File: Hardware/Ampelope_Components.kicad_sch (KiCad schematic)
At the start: 101 parts, among them J1 Conn_01x12_Male, J18 SWD_Header, J19 USB_B_Micro, J2 Conn_01x12_Male, J3 Conn_01x12_Male, J4 Conn_01x12_Male, J5 Eurorack_16_pin_power, Q1 MMBT3904, Q2 MMBT3904, Q3 MMBT3904, Q4 MMBT3904, Q5 MMBT3904, U1 STM32G431RB, U2 AS3364, U3 LM1117-3.3, U4 TL074, U5 TL074, U6 TL074, Y1 8MHz 20pF

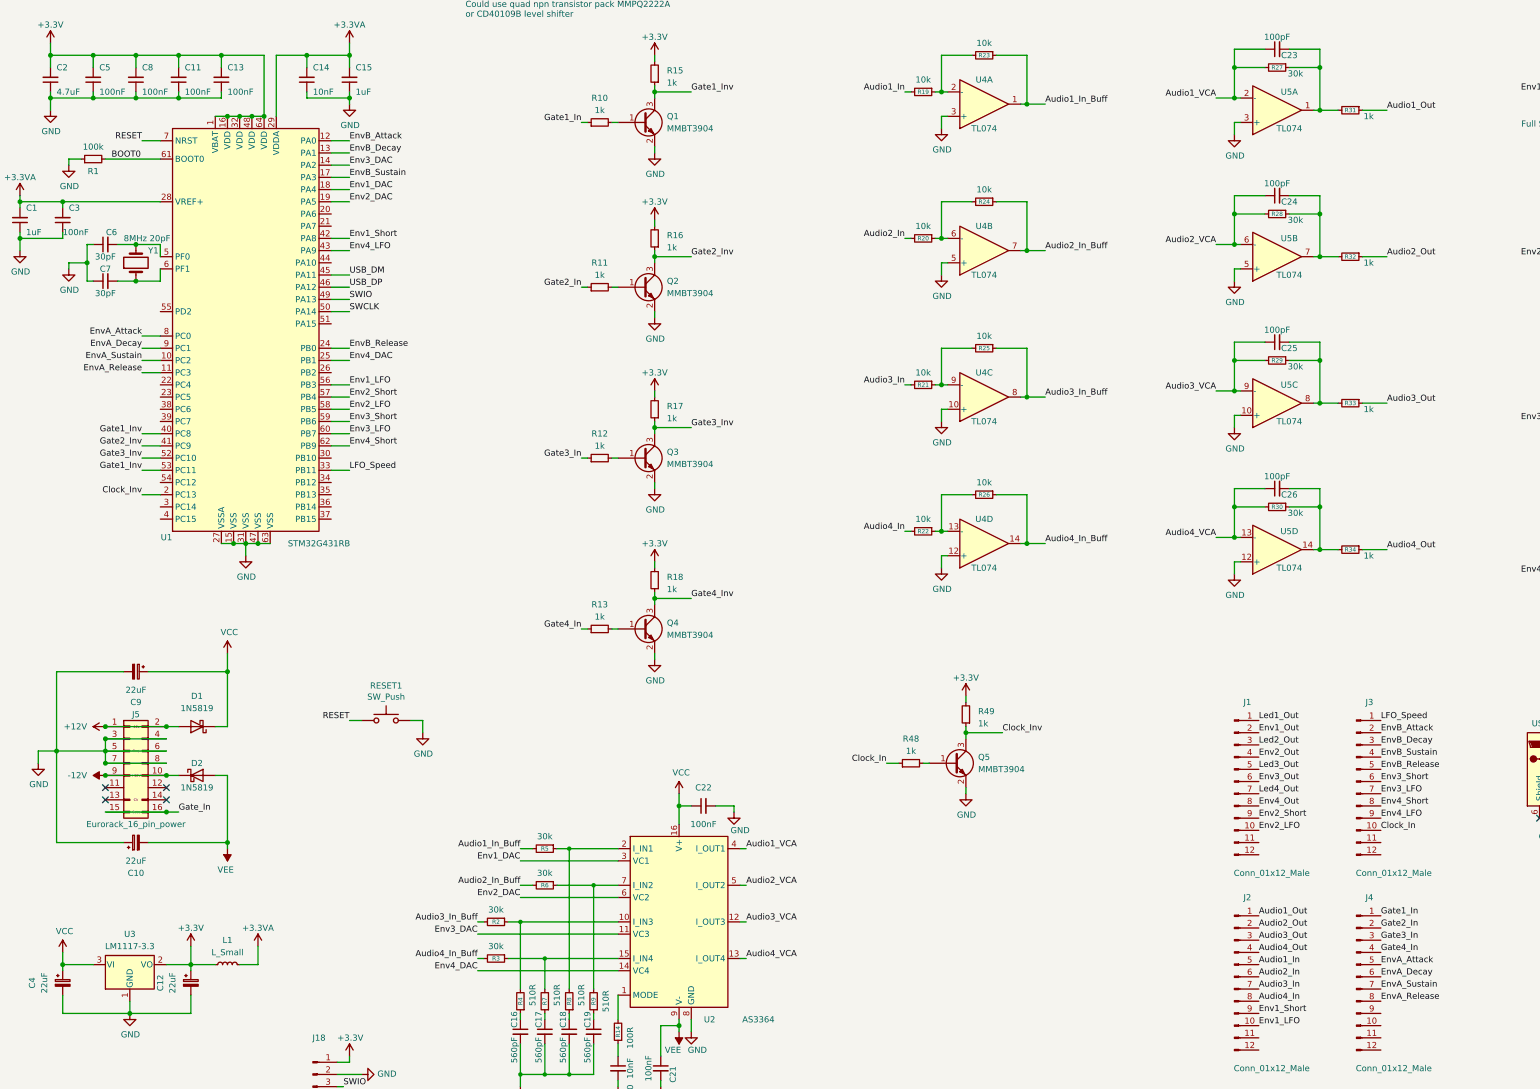
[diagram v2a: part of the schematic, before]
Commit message: More layout on component board
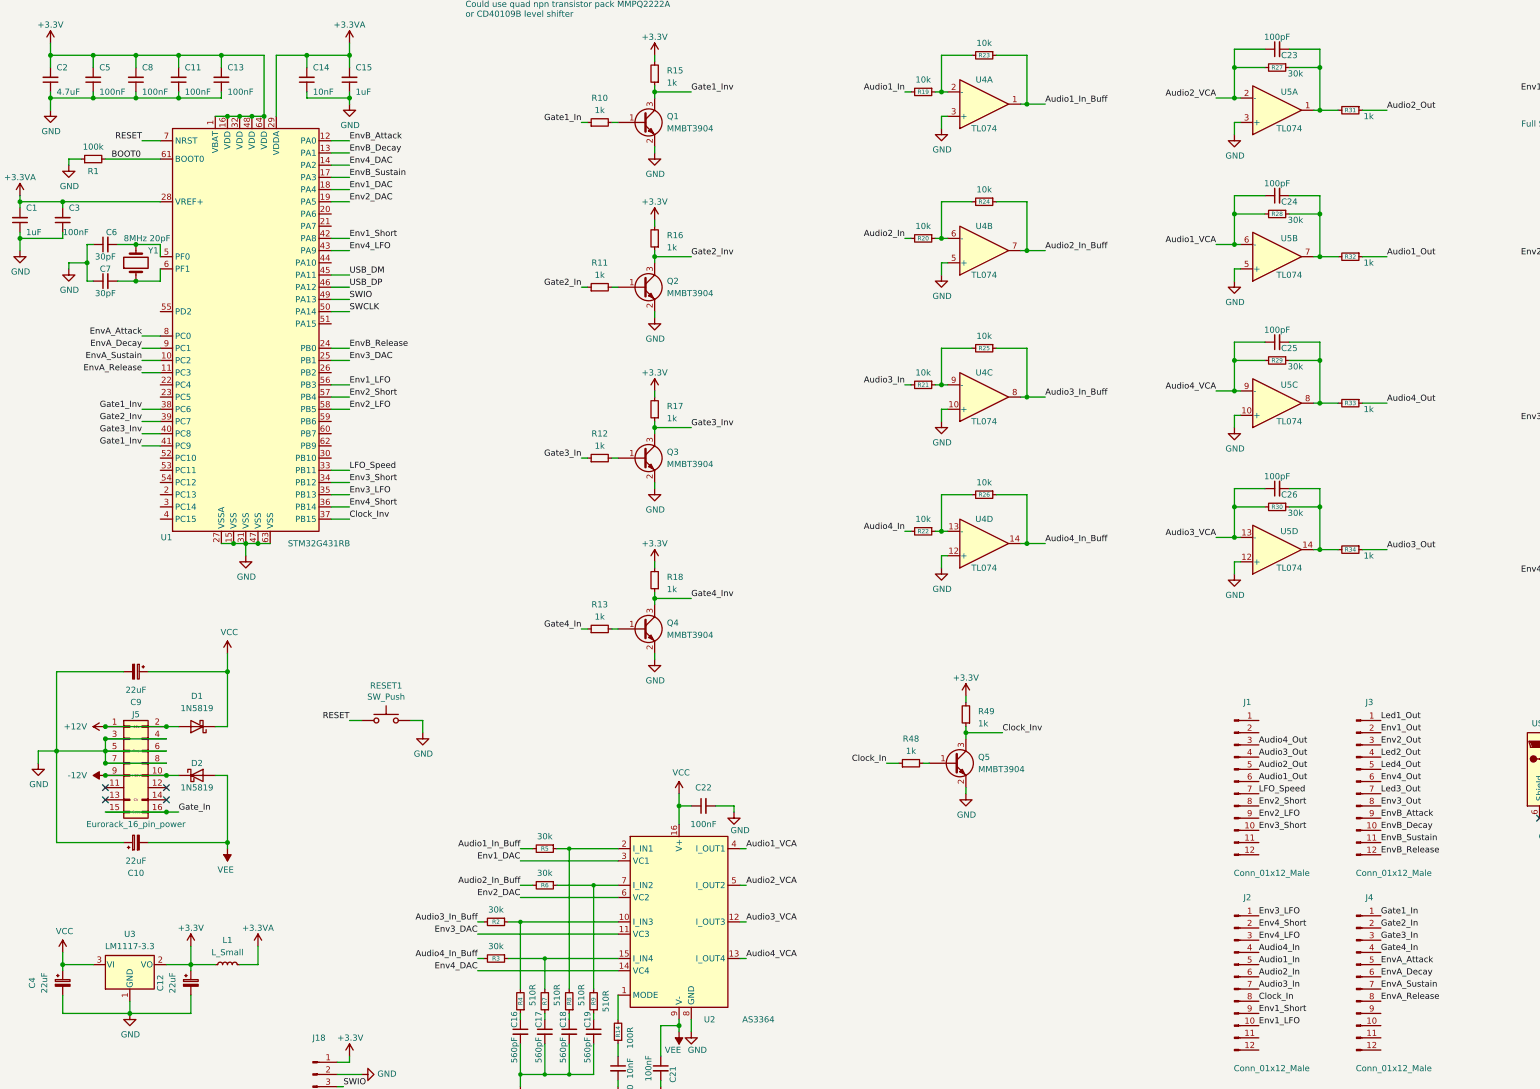
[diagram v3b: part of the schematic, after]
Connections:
- net Audio1_Out: now also J1.6 (Pin_6), R32.1; no longer J2.1 (Pin_1), R31.1
- net Audio1_VCA: now also C24.1, R28.2, U5.6 (-); no longer C23.1, R27.2, U5.2 (-)
- net Audio2_Out: now also J1.5 (Pin_5), R31.1; no longer J2.2 (Pin_2), R32.1
- net Audio2_VCA: now also C23.1, R27.2, U5.2 (-); no longer C24.1, R28.2, U5.6 (-)
- net Audio3_Out: now also J1.4 (Pin_4), R34.1; no longer J2.3 (Pin_3), R33.1
- net Audio3_VCA: now also C26.1, R30.2, U5.13 (-); no longer C25.1, R29.2, U5.9 (-)
- net Audio4_In: now also J2.4 (Pin_4); no longer J2.8 (Pin_8)
- net Audio4_Out: now also J1.3 (Pin_3), R33.1; no longer J2.4 (Pin_4), R34.1
- net Audio4_VCA: now also C25.1, R29.2, U5.9 (-); no longer C26.1, R30.2, U5.13 (-)
- net Clock_In: now also J2.8 (Pin_8); no longer J3.10 (Pin_10)
- net Clock_Inv: now also U1.37 (PB15); no longer U1.2 (PC13)
- net Env1_Out: now also J3.2 (Pin_2); no longer J1.2 (Pin_2)
- net Env2_LFO: now also J1.9 (Pin_9); no longer J1.10 (Pin_10)
- net Env2_Out: now also J3.3 (Pin_3); no longer J1.4 (Pin_4)
- net Env2_Short: now also J1.8 (Pin_8); no longer J1.9 (Pin_9)
- net Env3_DAC: now also U1.25 (PB1); no longer U1.14 (PA2)
- net Env3_LFO: now also J2.1 (Pin_1), U1.35 (PB13); no longer J3.7 (Pin_7), U1.60 (PB7)
- net Env3_Out: now also J3.8 (Pin_8); no longer J1.6 (Pin_6)
- net Env3_Short: now also J1.10 (Pin_10), U1.34 (PB12); no longer J3.6 (Pin_6), U1.59 (PB6)
- net Env4_DAC: now also U1.14 (PA2); no longer U1.25 (PB1)
- net Env4_LFO: now also J2.3 (Pin_3); no longer J3.9 (Pin_9)
- net Env4_Out: now also J3.6 (Pin_6); no longer J1.8 (Pin_8)
- net Env4_Short: now also J2.2 (Pin_2), U1.36 (PB14); no longer J3.8 (Pin_8), U1.62 (PB9)
- net EnvB_Attack: now also J3.9 (Pin_9); no longer J3.2 (Pin_2)
- net EnvB_Decay: now also J3.10 (Pin_10); no longer J3.3 (Pin_3)
- net EnvB_Release: now also J3.12 (Pin_12); no longer J3.5 (Pin_5)
- net EnvB_Sustain: now also J3.11 (Pin_11); no longer J3.4 (Pin_4)
- net Gate1_Inv: now also U1.38 (PC6), U1.41 (PC9); no longer U1.40 (PC8), U1.53 (PC11)
- net Gate2_Inv: now also U1.39 (PC7); no longer U1.41 (PC9)
- net Gate3_Inv: now also U1.40 (PC8); no longer U1.52 (PC10)
- net LFO_Speed: now also J1.7 (Pin_7); no longer J3.1 (Pin_1)
- net Led1_Out: now also J3.1 (Pin_1); no longer J1.1 (Pin_1)
- net Led2_Out: now also J3.4 (Pin_4); no longer J1.3 (Pin_3)
- net Led3_Out: now also J3.7 (Pin_7); no longer J1.5 (Pin_5)
- net Led4_Out: now also J3.5 (Pin_5); no longer J1.7 (Pin_7)

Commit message: More component layout
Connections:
- net Audio1_In: now also J2.1 (Pin_1); no longer J2.5 (Pin_5)
- net Audio2_In: now also J2.3 (Pin_3); no longer J2.6 (Pin_6)
- net Audio3_In: now also J2.4 (Pin_4); no longer J2.7 (Pin_7)
- net Audio4_In: now also J2.2 (Pin_2); no longer J2.4 (Pin_4)
- net Clock_In: now also J2.5 (Pin_5); no longer J2.8 (Pin_8)
- net Clock_Inv: now also U1.43 (PA9); no longer U1.37 (PB15)
- net Env1_LFO: now also J2.11 (Pin_11); no longer J2.10 (Pin_10)
- net Env1_Short: no longer J2.9 (Pin_9)
- net Env2_LFO: now also J4.6 (Pin_6); no longer J1.9 (Pin_9)
- net Env2_Short: now also J4.5 (Pin_5); no longer J1.8 (Pin_8)
- net Env3_LFO: now also J2.8 (Pin_8); no longer J2.1 (Pin_1)
- net Env3_Short: now also J2.7 (Pin_7); no longer J1.10 (Pin_10)
- net Env4_LFO: now also J2.10 (Pin_10), U1.37 (PB15); no longer J2.3 (Pin_3), U1.43 (PA9)
- net Env4_Short: now also J2.9 (Pin_9); no longer J2.2 (Pin_2)
- net EnvA_Attack: now also J4.1 (Pin_1); no longer J4.5 (Pin_5)
- net EnvA_Decay: now also J4.2 (Pin_2); no longer J4.6 (Pin_6)
- net EnvA_Release: now also J4.4 (Pin_4); no longer J4.8 (Pin_8)
- net EnvA_Sustain: now also J4.3 (Pin_3); no longer J4.7 (Pin_7)
- net Gate1_In: now also J4.7 (Pin_7); no longer J4.1 (Pin_1)
- net Gate1_Inv: no longer U1.41 (PC9)
- net Gate2_In: now also J4.8 (Pin_8); no longer J4.2 (Pin_2)
- net Gate3_In: now also J4.9 (Pin_9); no longer J4.3 (Pin_3)
- net Gate4_In: now also J4.10 (Pin_10); no longer J4.4 (Pin_4)
- net Gate4_Inv: now also U1.41 (PC9)
- net LFO_Speed: now also J2.6 (Pin_6); no longer J1.7 (Pin_7)
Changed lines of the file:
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@@
     (effects (font (size 1.27 1.27)) (justify right bottom))
   )
-  (label "Gate1_Inv" (at 45.72 110.49 180)
+  (label "Gate4_Inv" (at 45.72 110.49 180)
     (effects (font (size 1.27 1.27)) (justify right bottom))
   )
@@
     (effects (font (size 1.27 1.27)) (justify left bottom))
   )
-  (label "Env4_LFO" (at 88.9 69.85 0)
+  (label "Clock_Inv" (at 88.9 69.85 0)
     (effects (font (size 1.27 1.27)) (justify left bottom))
   )
@@
     (effects (font (size 1.27 1.27)) (justify left bottom))
   )
-  (label "Clock_Inv" (at 88.9 125.73 0)
+  (label "Env4_LFO" (at 88.9 125.73 0)
     (effects (font (size 1.27 1.27)) (justify left bottom))
   )
@@
     (effects (font (size 1.27 1.27)) (justify left bottom))
   )
+  (label "Env1_Short" (at 255.27 226.06 0)
+    (effects (font (size 1.27 1.27)) (justify left bottom))
+  )
   (label "Audio2_VCA" (at 269.24 38.1 180)
     (effects (font (size 1.27 1.27)) (justify right bottom))
@@
     (effects (font (size 1.27 1.27)) (justify left bottom))
   )
-  (label "LFO_Speed" (at 278.13 182.88 0)
-    (effects (font (size 1.27 1.27)) (justify left bottom))
-  )
-  (label "Env2_Short" (at 278.13 185.42 0)
-    (effects (font (size 1.27 1.27)) (justify left bottom))
-  )
-  (label "Env2_LFO" (at 278.13 187.96 0)
-    (effects (font (size 1.27 1.27)) (justify left bottom))
-  )
-  (label "Env3_Short" (at 278.13 190.5 0)
-    (effects (font (size 1.27 1.27)) (justify left bottom))
-  )
-  (label "Env3_LFO" (at 278.13 208.28 0)
-    (effects (font (size 1.27 1.27)) (justify left bottom))
-  )
-  (label "Env4_Short" (at 278.13 210.82 0)
-    (effects (font (size 1.27 1.27)) (justify left bottom))
-  )
-  (label "Env4_LFO" (at 278.13 213.36 0)
-    (effects (font (size 1.27 1.27)) (justify left bottom))
-  )
-  (label "Audio4_In" (at 278.13 215.9 0)
-    (effects (font (size 1.27 1.27)) (justify left bottom))
-  )
-  (label "Audio1_In" (at 278.13 218.44 0)
-    (effects (font (size 1.27 1.27)) (justify left bottom))
-  )
-  (label "Audio2_In" (at 278.13 220.98 0)
-    (effects (font (size 1.27 1.27)) (justify left bottom))
-  )
-  (label "Audio3_In" (at 278.13 223.52 0)
-    (effects (font (size 1.27 1.27)) (justify left bottom))
-  )
-  (label "Clock_In" (at 278.13 226.06 0)
-    (effects (font (size 1.27 1.27)) (justify left bottom))
-  )
-  (label "Env1_Short" (at 278.13 228.6 0)
-    (effects (font (size 1.27 1.27)) (justify left bottom))
-  )
-  (label "Env1_LFO" (at 278.13 231.14 0)
+  (label "Audio1_In" (at 278.13 208.28 0)
+    (effects (font (size 1.27 1.27)) (justify left bottom))
+  )
+  (label "Audio4_In" (at 278.13 210.82 0)
+    (effects (font (size 1.27 1.27)) (justify left bottom))
+  )
+  (label "Audio2_In" (at 278.13 213.36 0)
+    (effects (font (size 1.27 1.27)) (justify left bottom))
+  )
+  (label "Audio3_In" (at 278.13 215.9 0)
+    (effects (font (size 1.27 1.27)) (justify left bottom))
+  )
+  (label "Clock_In" (at 278.13 218.44 0)
+    (effects (font (size 1.27 1.27)) (justify left bottom))
+  )
+  (label "LFO_Speed" (at 278.13 220.98 0)
+    (effects (font (size 1.27 1.27)) (justify left bottom))
+  )
+  (label "Env3_Short" (at 278.13 223.52 0)
+    (effects (font (size 1.27 1.27)) (justify left bottom))
+  )
+  (label "Env3_LFO" (at 278.13 226.06 0)
+    (effects (font (size 1.27 1.27)) (justify left bottom))
+  )
+  (label "Env4_Short" (at 278.13 228.6 0)
+    (effects (font (size 1.27 1.27)) (justify left bottom))
+  )
+  (label "Env4_LFO" (at 278.13 231.14 0)
+    (effects (font (size 1.27 1.27)) (justify left bottom))
+  )
+  (label "Env1_LFO" (at 278.13 233.68 0)
     (effects (font (size 1.27 1.27)) (justify left bottom))
   )
@@
     (effects (font (size 1.27 1.27)) (justify left bottom))
   )
-  (label "Gate1_In" (at 303.53 208.28 0)
-    (effects (font (size 1.27 1.27)) (justify left bottom))
-  )
-  (label "Gate2_In" (at 303.53 210.82 0)
-    (effects (font (size 1.27 1.27)) (justify left bottom))
-  )
-  (label "Gate3_In" (at 303.53 213.36 0)
-    (effects (font (size 1.27 1.27)) (justify left bottom))
-  )
-  (label "Gate4_In" (at 303.53 215.9 0)
-    (effects (font (size 1.27 1.27)) (justify left bottom))
-  )
-  (label "EnvA_Attack" (at 303.53 218.44 0)
-    (effects (font (size 1.27 1.27)) (justify left bottom))
-  )
-  (label "EnvA_Decay" (at 303.53 220.98 0)
-    (effects (font (size 1.27 1.27)) (justify left bottom))
-  )
-  (label "EnvA_Sustain" (at 303.53 223.52 0)
-    (effects (font (size 1.27 1.27)) (justify left bottom))
-  )
-  (label "EnvA_Release" (at 303.53 226.06 0)
-    (effects (font (size 1.27 1.27)) (justify left bottom))
-  )
+  (label "EnvA_Attack" (at 303.53 208.28 0)
+    (effects (font (size 1.27 1.27)) (justify left bottom))
+  )
+  (label "EnvA_Decay" (at 303.53 210.82 0)
+    (effects (font (size 1.27 1.27)) (justify left bottom))
+  )
+  (label "EnvA_Sustain" (at 303.53 213.36 0)
+    (effects (font (size 1.27 1.27)) (justify left bottom))
+  )
+  (label "EnvA_Release" (at 303.53 215.9 0)
+    (effects (font (size 1.27 1.27)) (justify left bottom))
+  )
+  (label "Env2_Short" (at 303.53 218.44 0)
+    (effects (font (size 1.27 1.27)) (justify left bottom))
+  )
+  (label "Env2_LFO" (at 303.53 220.98 0)
+    (effects (font (size 1.27 1.27)) (justify left bottom))
+  )
+  (label "Gate1_In" (at 303.53 223.52 0)
+    (effects (font (size 1.27 1.27)) (justify left bottom))
+  )
+  (label "Gate2_In" (at 303.53 226.06 0)
+    (effects (font (size 1.27 1.27)) (justify left bottom))
+  )
+  (label "Gate3_In" (at 303.53 228.6 0)
+    (effects (font (size 1.27 1.27)) (justify left bottom))
+  )
+  (label "Gate4_In" (at 303.53 231.14 0)
+    (effects (font (size 1.27 1.27)) (justify left bottom))
+  )
